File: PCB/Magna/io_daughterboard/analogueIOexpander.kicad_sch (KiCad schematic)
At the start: 2 parts, among them U1501 4052

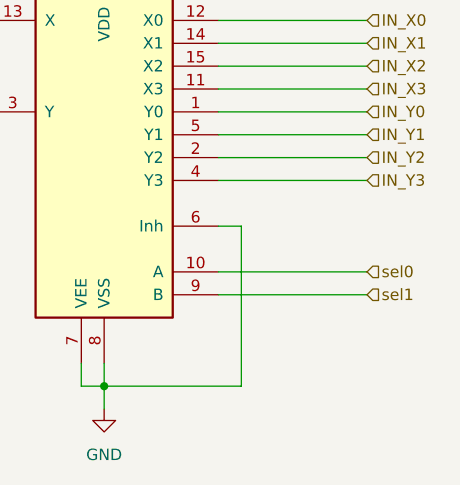
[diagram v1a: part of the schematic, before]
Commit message: Add a lot on the IO PCB
Also some schematic changes to accomodate issues found
when routing
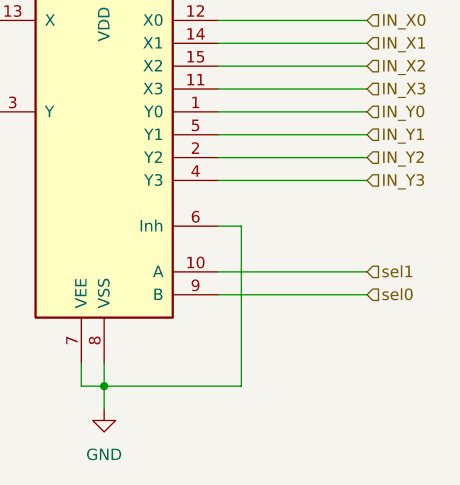
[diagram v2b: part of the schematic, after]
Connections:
- net sel0: now also U1501.9 (B); no longer U1501.10 (A)
- net sel1: now also U1501.10 (A); no longer U1501.9 (B)
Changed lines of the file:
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@@
     (effects (font (size 1.27 1.27)) (justify left))
   )
-  (hierarchical_label "sel0" (shape input) (at 166.37 113.03 0) (fields_autoplaced)
+  (hierarchical_label "sel0" (shape input) (at 166.37 115.57 0) (fields_autoplaced)
     (effects (font (size 1.27 1.27)) (justify left))
   )
@@
     (effects (font (size 1.27 1.27)) (justify left))
   )
-  (hierarchical_label "sel1" (shape input) (at 166.37 115.57 0) (fields_autoplaced)
+  (hierarchical_label "sel1" (shape input) (at 166.37 113.03 0) (fields_autoplaced)
     (effects (font (size 1.27 1.27)) (justify left))
   )

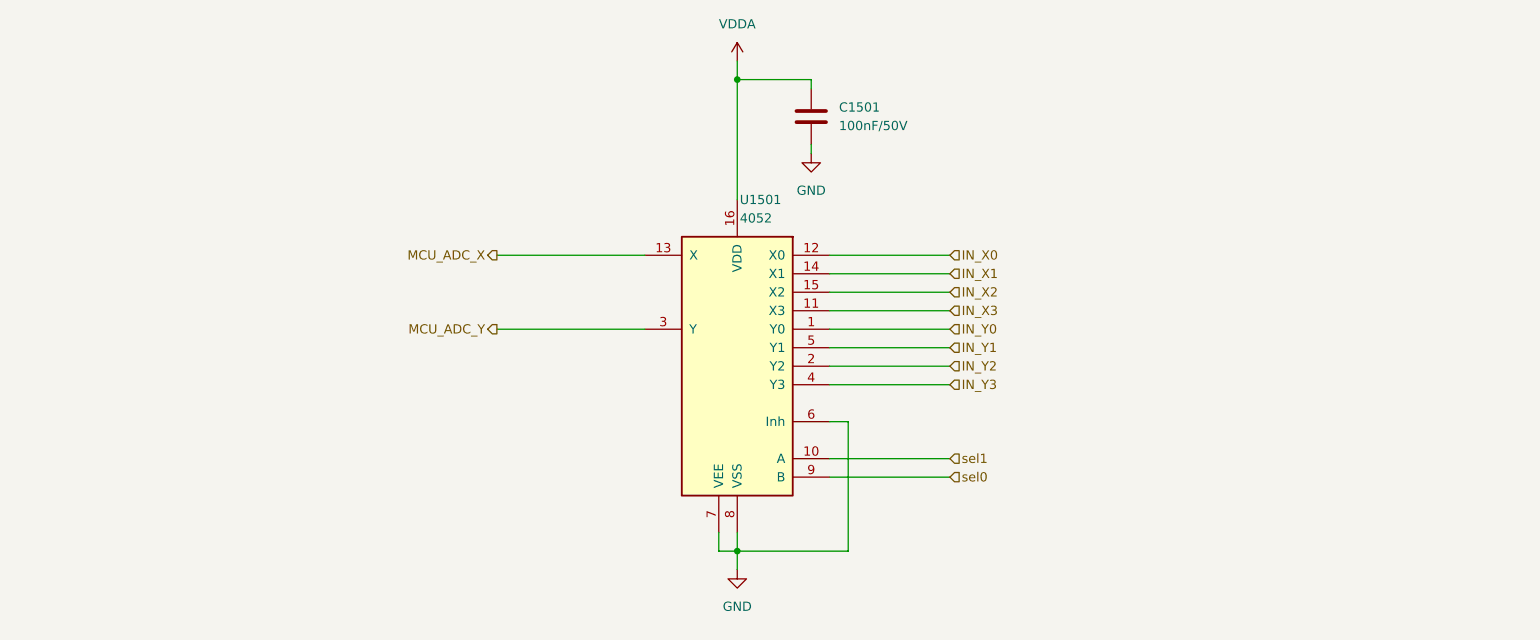
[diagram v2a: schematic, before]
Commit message: Add more routing to IO Daugherboard
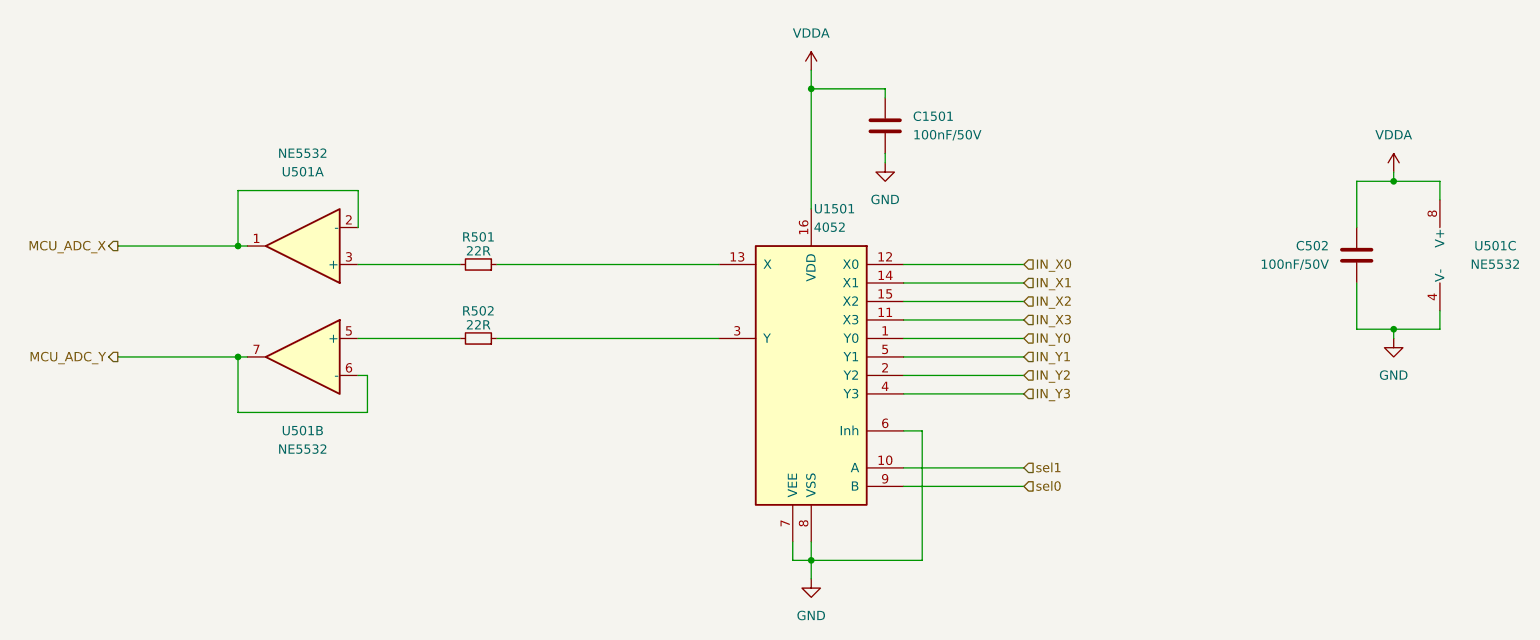
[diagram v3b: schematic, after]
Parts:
- added C502: 100nF/50V, Capacitor_SMD:C_0805_2012Metric_Pad1.18x1.45mm_HandSolder, symbol Device:C
- added R501, R502: 22R, Resistor_SMD:R_0805_2012Metric_Pad1.20x1.40mm_HandSolder, symbol Device:R_Small
- added U501: NE5532, Package_SO:SOIC-8_3.9x4.9mm_P1.27mm, symbol Amplifier_Operational:NE5532
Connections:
- net GND: now also C502.2, U501.4 (V-)
- net MCU_ADC_X: now also U501.1, U501.2 (-); no longer U1501.13 (X)
- net MCU_ADC_Y: now also U501.6 (-), U501.7; no longer U1501.3 (Y)
- net VDDA: now also C502.1, U501.8 (V+)
- new net: R501.2, U501.3 (+)
- new net: R502.2, U501.5 (+)
- new net: R502.1, U1501.3 (Y)
- new net: R501.1, U1501.13 (X)
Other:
- moved on the sheet: C1501, U1501

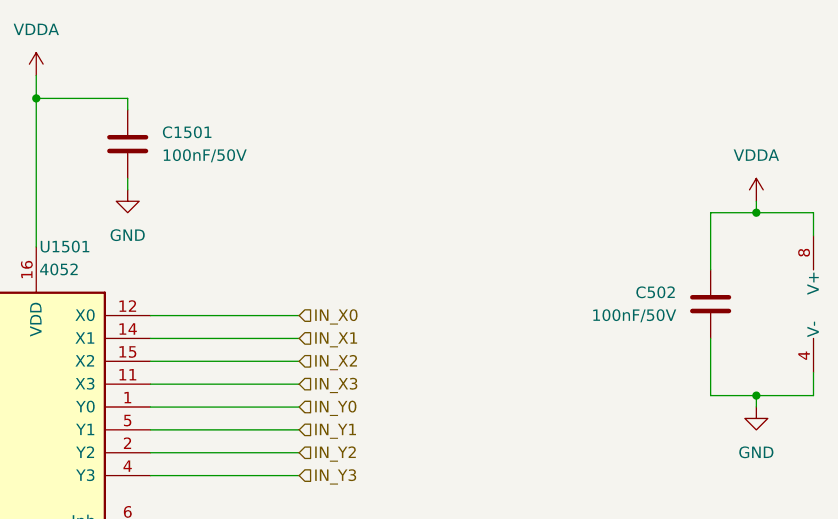
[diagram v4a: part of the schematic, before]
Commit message: Change all capacitors to 22uF on IO board(#5)
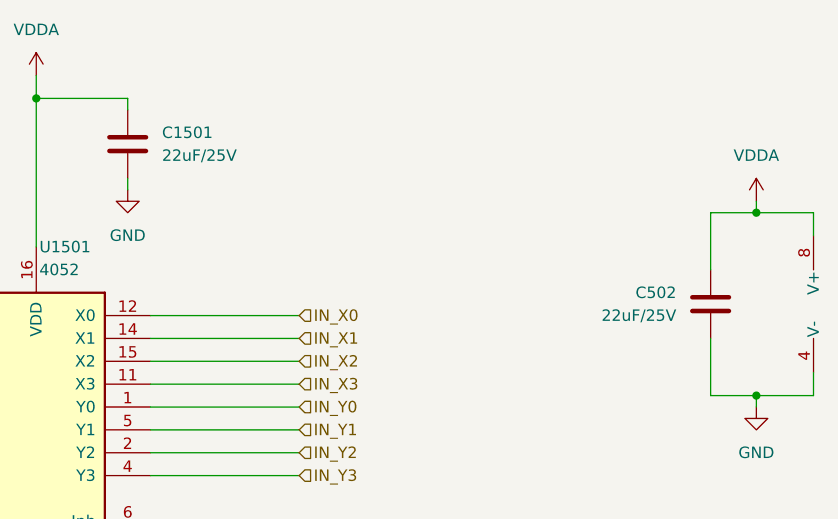
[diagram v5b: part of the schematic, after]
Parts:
- C1501, C502: value 100nF/50V -> 22uF/25V; LCSC C49678 -> C45783
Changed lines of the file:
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@@
       (effects (font (size 1.27 1.27)) (justify left))
     )
-    (property "Value" "100nF/50V" (at 218.44 86.36 0)
+    (property "Value" "22uF/25V" (at 218.44 86.36 0)
       (effects (font (size 1.27 1.27)) (justify left))
     )
@@
       (effects (font (size 1.27 1.27)) hide)
     )
-    (property "LCSC" "C49678" (at 222.25 85.09 0)
+    (property "LCSC" "C45783" (at 222.25 85.09 0)
       (effects (font (size 1.27 1.27)) hide)
     )
@@
       (effects (font (size 1.27 1.27)) (justify left))
     )
-    (property "Value" "100nF/50V" (at 161.29 68.58 0)
+    (property "Value" "22uF/25V" (at 161.29 68.58 0)
       (effects (font (size 1.27 1.27)) (justify left))
     )
@@
       (effects (font (size 1.27 1.27)) hide)
     )
-    (property "LCSC" "C49678" (at 157.48 67.31 0)
+    (property "LCSC" "C45783" (at 157.48 67.31 0)
       (effects (font (size 1.27 1.27)) hide)
     )

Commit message: Update some files to KiCad8 and make ready for production
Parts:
- U1501: footprint Package_SO:SO-16_3.9x9.9mm_P1.27mm -> Package_SO:SOIC-16_3.9x9.9mm_P1.27mm; LCSC C11350 -> C6521

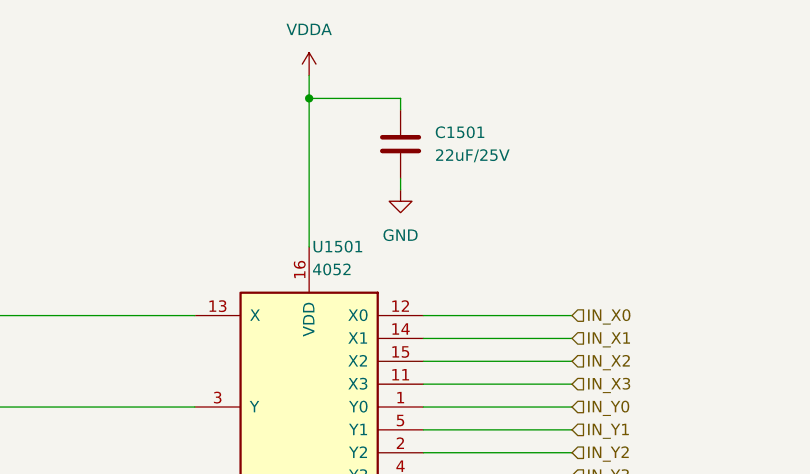
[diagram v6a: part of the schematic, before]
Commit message: Update Project to Kicad 8.0 and prepare for production
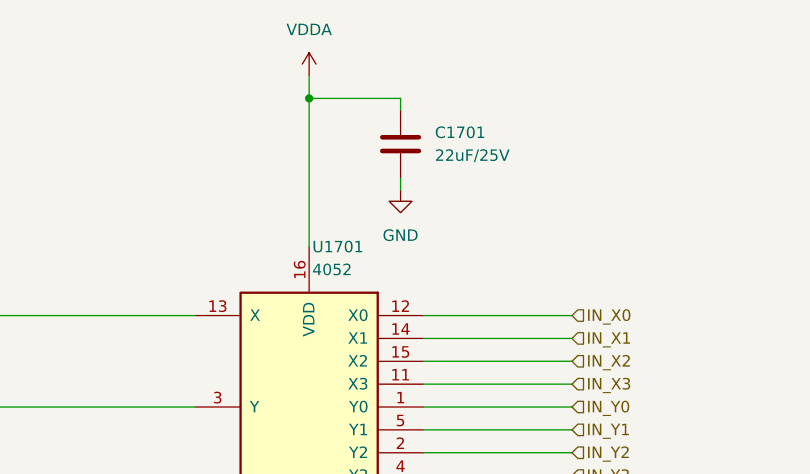
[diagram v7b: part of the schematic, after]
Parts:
- renumbered C1501 to C1701, U1501 to U1701
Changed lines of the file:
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@@
 			)
 		)
-		(property "Description" ""
+		(property "Description" "Dual Low-Noise Operational Amplifiers, DIP-8/SOIC-8"
 			(at 231.14 85.09 0)
 			(effects
@@
 			)
 		)
-		(property "Description" ""
+		(property "Description" "Dual Low-Noise Operational Amplifiers, DIP-8/SOIC-8"
 			(at 77.47 83.82 0)
 			(effects
@@
 			)
 		)
-		(property "Description" ""
+		(property "Description" "Unpolarized capacitor"
 			(at 222.25 85.09 0)
 			(effects
@@
 			)
 		)
-		(property "Description" ""
+		(property "Description" "Dual Low-Noise Operational Amplifiers, DIP-8/SOIC-8"
 			(at 77.47 99.06 0)
 			(effects
@@
 			)
 		)
-		(property "Description" ""
+		(property "Description" "Resistor, small symbol"
 			(at 101.6 96.52 0)
 			(effects
@@
 			)
 		)
-		(property "Description" ""
+		(property "Description" "Power symbol creates a global label with name \"VDDA\""
 			(at 227.33 73.66 0)
 			(effects
@@
 		(dnp no)
 		(fields_autoplaced yes)
-		(property "Reference" "#PWR01503"
+		(property "Reference" "#PWR01703"
 			(at 157.48 78.74 0)
 			(effects
@@
 			)
 		)
-		(property "Description" ""
+		(property "Description" "Power symbol creates a global label with name \"GND\" , ground"
 			(at 157.48 72.39 0)
 			(effects
@@
 		(dnp no)
 		(fields_autoplaced yes)
-		(property "Reference" "C1501"
+		(property "Reference" "C1701"
 			(at 161.29 66.04 0)
 			(effects
@@
 			)
 		)
-		(property "Description" ""
+		(property "Description" "Unpolarized capacitor"
 			(at 157.48 67.31 0)
 			(effects
@@
 			)
 		)
-		(property "Description" ""
+		(property "Description" "Resistor, small symbol"
 			(at 101.6 86.36 0)
 			(effects
@@
 		(on_board yes)
 		(dnp no)
-		(property "Reference" "U1501"
+		(property "Reference" "U1701"
 			(at 147.6659 78.74 0)
 			(effects
@@
 			)
 		)
-		(property "Description" ""
+		(property "Description" "Dual Analog Multiplexer 4 to 1 line"
 			(at 147.32 101.6 0)
 			(effects
@@
 		(dnp no)
 		(fields_autoplaced yes)
-		(property "Reference" "#PWR01502"
+		(property "Reference" "#PWR01702"
 			(at 147.32 135.89 0)
 			(effects
@@
 			)
 		)
-		(property "Description" ""
+		(property "Description" "Power symbol creates a global label with name \"GND\" , ground"
 			(at 147.32 129.54 0)
 			(effects
@@
 			)
 		)
-		(property "Description" ""
+		(property "Description" "Power symbol creates a global label with name \"GND\" , ground"
 			(at 227.33 96.52 0)
 			(effects
@@
 		(dnp no)
 		(fields_autoplaced yes)
-		(property "Reference" "#PWR01501"
+		(property "Reference" "#PWR01701"
 			(at 147.32 63.5 0)
 			(effects
@@
 			)
 		)
-		(property "Description" ""
+		(property "Description" "Power symbol creates a global label with name \"VDDA\""
 			(at 147.32 59.69 0)
 			(effects

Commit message: Update schematics to Kicad 9
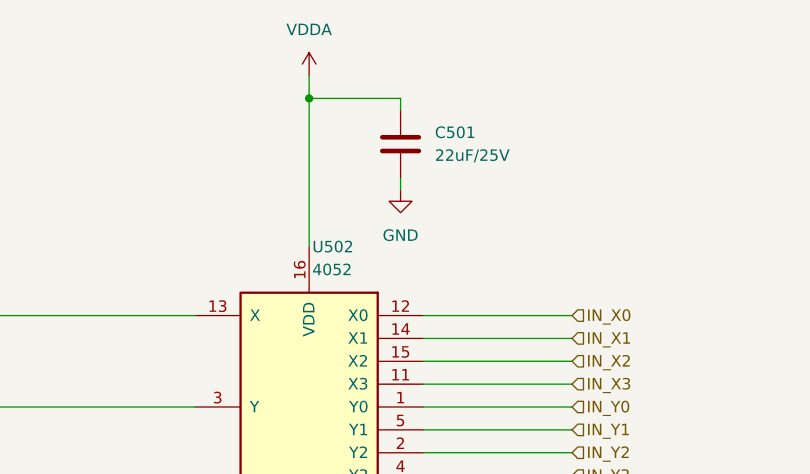
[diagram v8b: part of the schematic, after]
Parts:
- renumbered C1701 to C501, U1701 to U502
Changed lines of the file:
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@@
 (kicad_sch
-	(version 20231120)
+	(version 20250114)
 	(generator "eeschema")
-	(generator_version "8.0")
+	(generator_version "9.0")
 	(paper "A4")
 	(junction
@@
 		(shape input)
 		(at 176.53 91.44 0)
-		(fields_autoplaced yes)
 		(effects
 			(font
@@
 		(shape input)
 		(at 176.53 116.84 0)
-		(fields_autoplaced yes)
 		(effects
 			(font
@@
 		(shape output)
 		(at 52.07 99.06 180)
-		(fields_autoplaced yes)
 		(effects
 			(font
@@
 		(shape input)
 		(at 176.53 96.52 0)
-		(fields_autoplaced yes)
 		(effects
 			(font
@@
 		(shape input)
 		(at 176.53 93.98 0)
-		(fields_autoplaced yes)
 		(effects
 			(font
@@
 		(shape input)
 		(at 176.53 88.9 0)
-		(fields_autoplaced yes)
 		(effects
 			(font
@@
 		(shape input)
 		(at 176.53 86.36 0)
-		(fields_autoplaced yes)
 		(effects
 			(font
@@
 		(shape input)
 		(at 176.53 104.14 0)
-		(fields_autoplaced yes)
 		(effects
 			(font
@@
 		(shape input)
 		(at 176.53 114.3 0)
-		(fields_autoplaced yes)
 		(effects
 			(font
@@
 		(shape input)
 		(at 176.53 101.6 0)
-		(fields_autoplaced yes)
 		(effects
 			(font
@@
 		(shape output)
 		(at 52.07 83.82 180)
-		(fields_autoplaced yes)
 		(effects
 			(font
@@
 		(shape input)
 		(at 176.53 99.06 0)
-		(fields_autoplaced yes)
 		(effects
 			(font
@@
 		(dnp no)
 		(fields_autoplaced yes)
-		(property "Reference" "#PWR01703"
+		(property "Reference" "#PWR0503"
 			(at 157.48 78.74 0)
 			(effects
@@
 		(dnp no)
 		(fields_autoplaced yes)
-		(property "Reference" "C1701"
+		(property "Reference" "C501"
 			(at 161.29 66.04 0)
 			(effects
@@
 		(on_board yes)
 		(dnp no)
-		(property "Reference" "U1701"
+		(property "Reference" "U502"
 			(at 147.6659 78.74 0)
 			(effects
@@
 		(dnp no)
 		(fields_autoplaced yes)
-		(property "Reference" "#PWR01702"
+		(property "Reference" "#PWR0502"
 			(at 147.32 135.89 0)
 			(effects
@@
 		(dnp no)
 		(fields_autoplaced yes)
-		(property "Reference" "#PWR01701"
+		(property "Reference" "#PWR0501"
 			(at 147.32 63.5 0)
 			(effects
